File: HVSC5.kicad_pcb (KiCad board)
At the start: 2 copper layers, 220 x 152 mm, 336 parts, among them J1 test, J10 CONN_01X03, J11 test, J12 test, J13 test, J14 test, J15 test, J16 test, J17 CONN_COAXIAL, J18 CONN_01X03, J19 CONN_01X03, J2 test, J20 CONN_01X08, J21 test, J22 test, J23 test, J24 test, J25 CONN_01X05, J26 test, J27 test, J3 test, J4 test, J5 CONN_01X05, J6 test, J7 CONN_01X05, J8 CONN_COAXIAL, J9 DB9_Female_MountingHoles, SW1 SW_Push, U1 AD7175-8, U10 LT1118-5V, U11 FOD0721, U12 DPBW06, U13 LTC2644, U14 uA7805, U15 INA128, U16 XR2206, U17 TLP176A, U18 ANA4522, U19 ACPL-W343, U2 ADR4520, U20 ACPL-W343, U21 ANA4522, U3 ADR445, U4 74LS04, U5 dsPIC33EV256GM002, U6 SN75451, U7 MAX232, U8 HFBR-2412, U9 HFBR-1414, X1 P7002SCLRP, X2 P7002SCLRP, X3 P7002SCLRP, X4 P7002SCLRP, X5 P7002SCLRP, X6 P7002SCLRP, Y1 16M, Y2 8M

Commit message: Small_Change
시험삼아서 수정하였음
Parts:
- U2, U3: footprint Housings_SOIC:SOIC-8_3.9x4.9mm_Pitch1.27mm -> USER:SOIC-8_3.9x4.9mm_Pitch1.27mm
- moved J2 0.51 mm to (131.1, 79.5)
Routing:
- net /Monitor/Sine_output: track 59.2 -> 61.4 mm
- net Net-(R136-Pad1): track 15.2 -> 13.6 mm
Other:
- board text added: "+10V"
- board text added: "+1V"
- board text added: "+30V"
- board text added: "+600V"
- board text added: "-10V"
- board text added: "-1V"
- board text added: "-30V"
- board text added: "-600V"
- board text added: "Input+"
- board text added: "Input-"
- board text added: "Monitor"

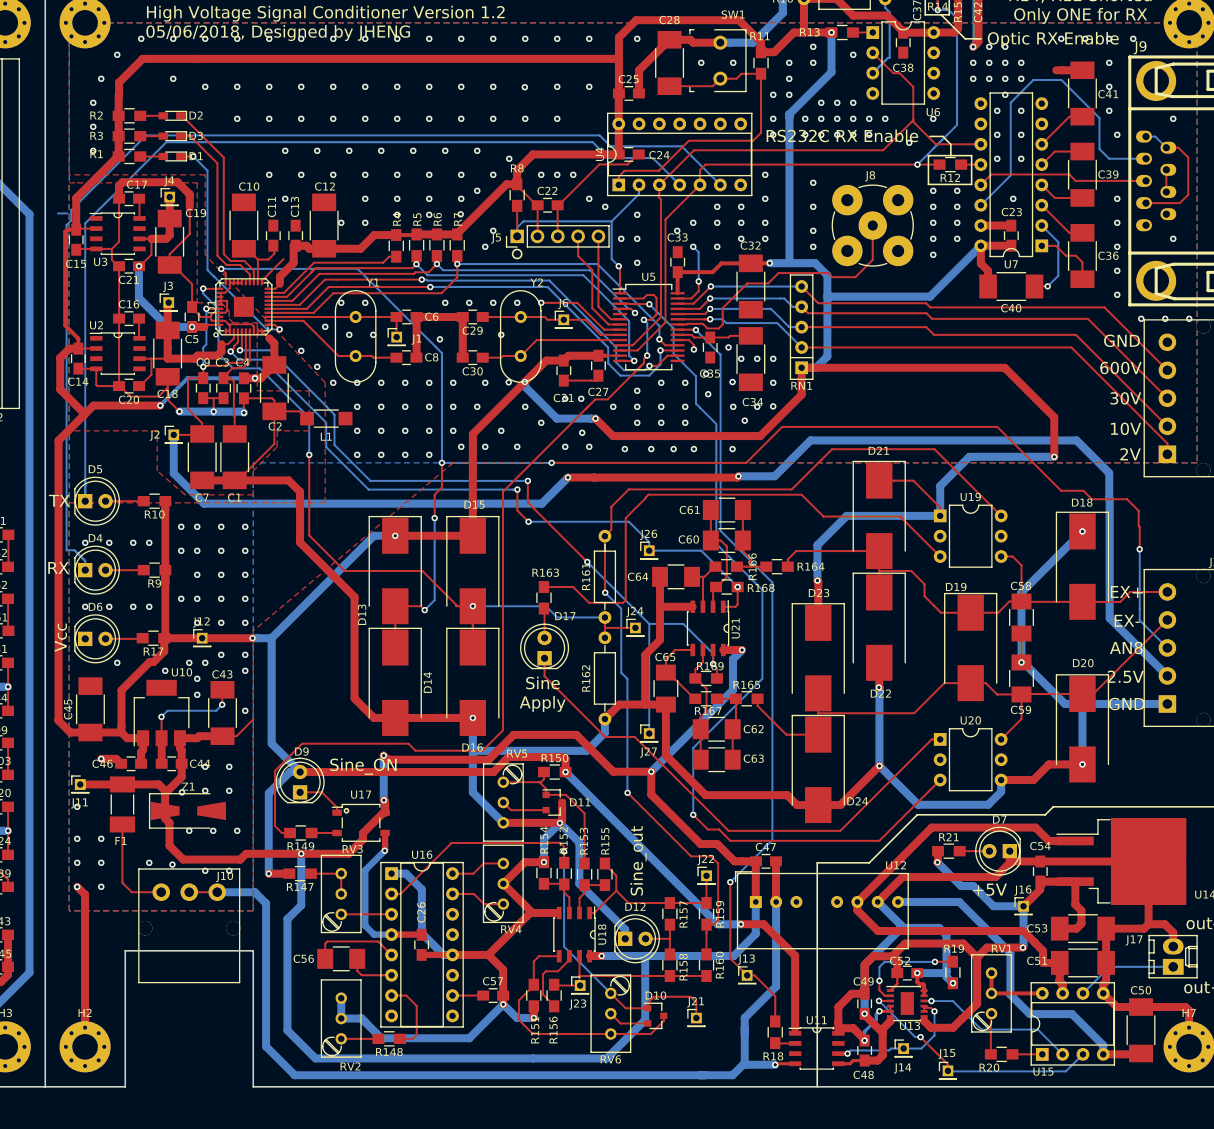
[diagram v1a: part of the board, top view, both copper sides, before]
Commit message: 전해콘덴서 foot print 변경
전해 콘덴서 변경
Bypass 콘데서 OPAMP에 추가 하여야 함
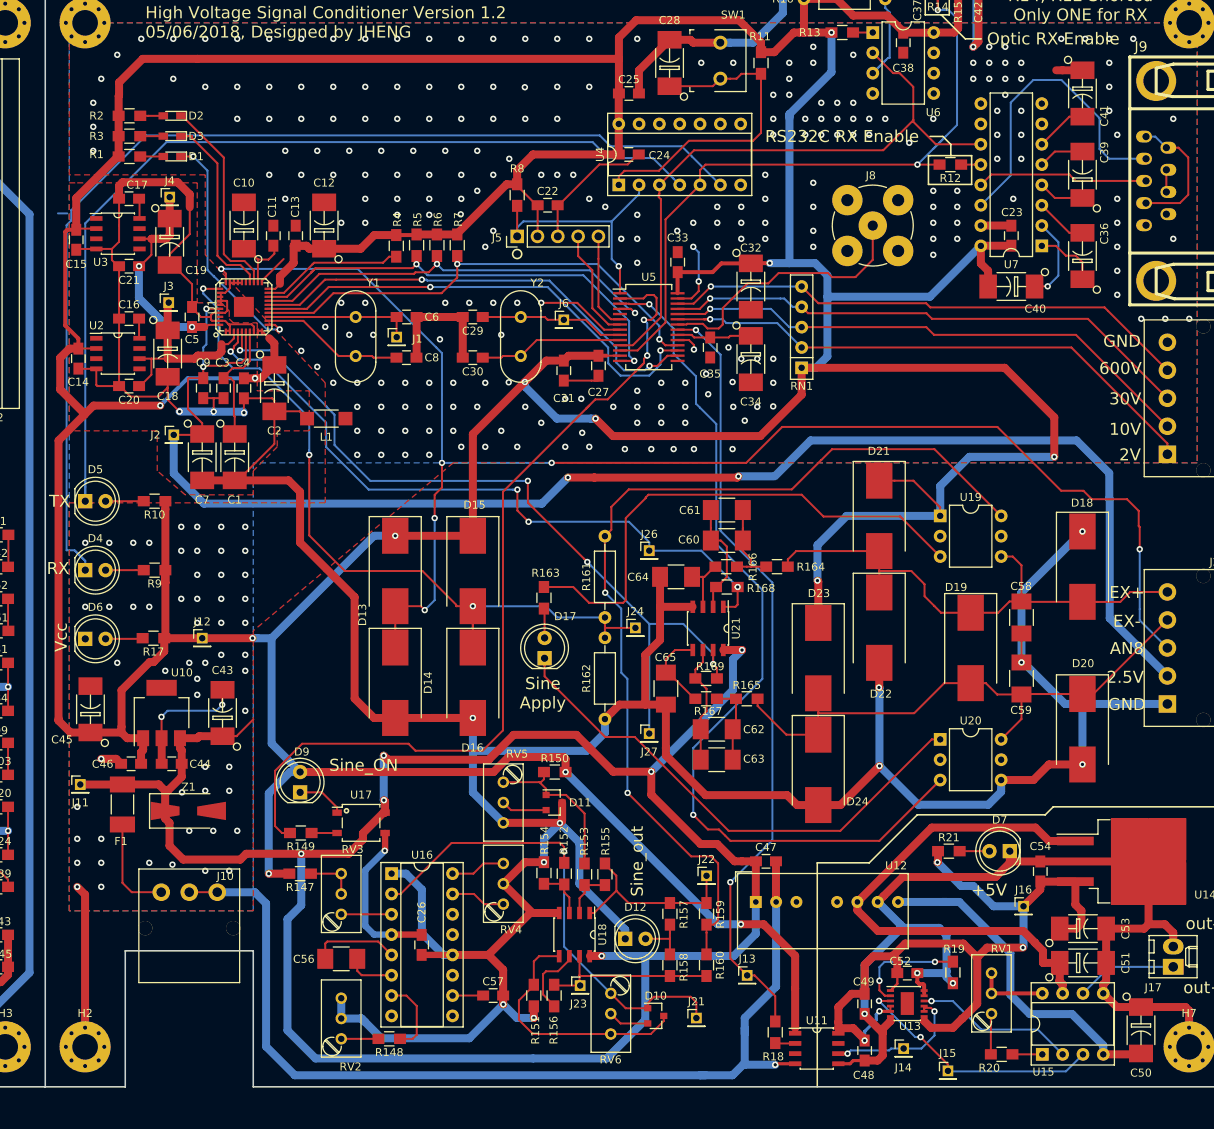
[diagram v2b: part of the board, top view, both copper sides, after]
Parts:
- C1, C10, C12, C18, C19, C2, C28, C32, C34, C36, C39, C40, C41, C43, C45, C50, C51, C53, C7: footprint Capacitors_SMD:C_1812_HandSoldering -> USER:C_1812_HandSoldering_Polar
- C55: value 0.1uF -> 10uF
- R159, R160: value 10k -> 1k

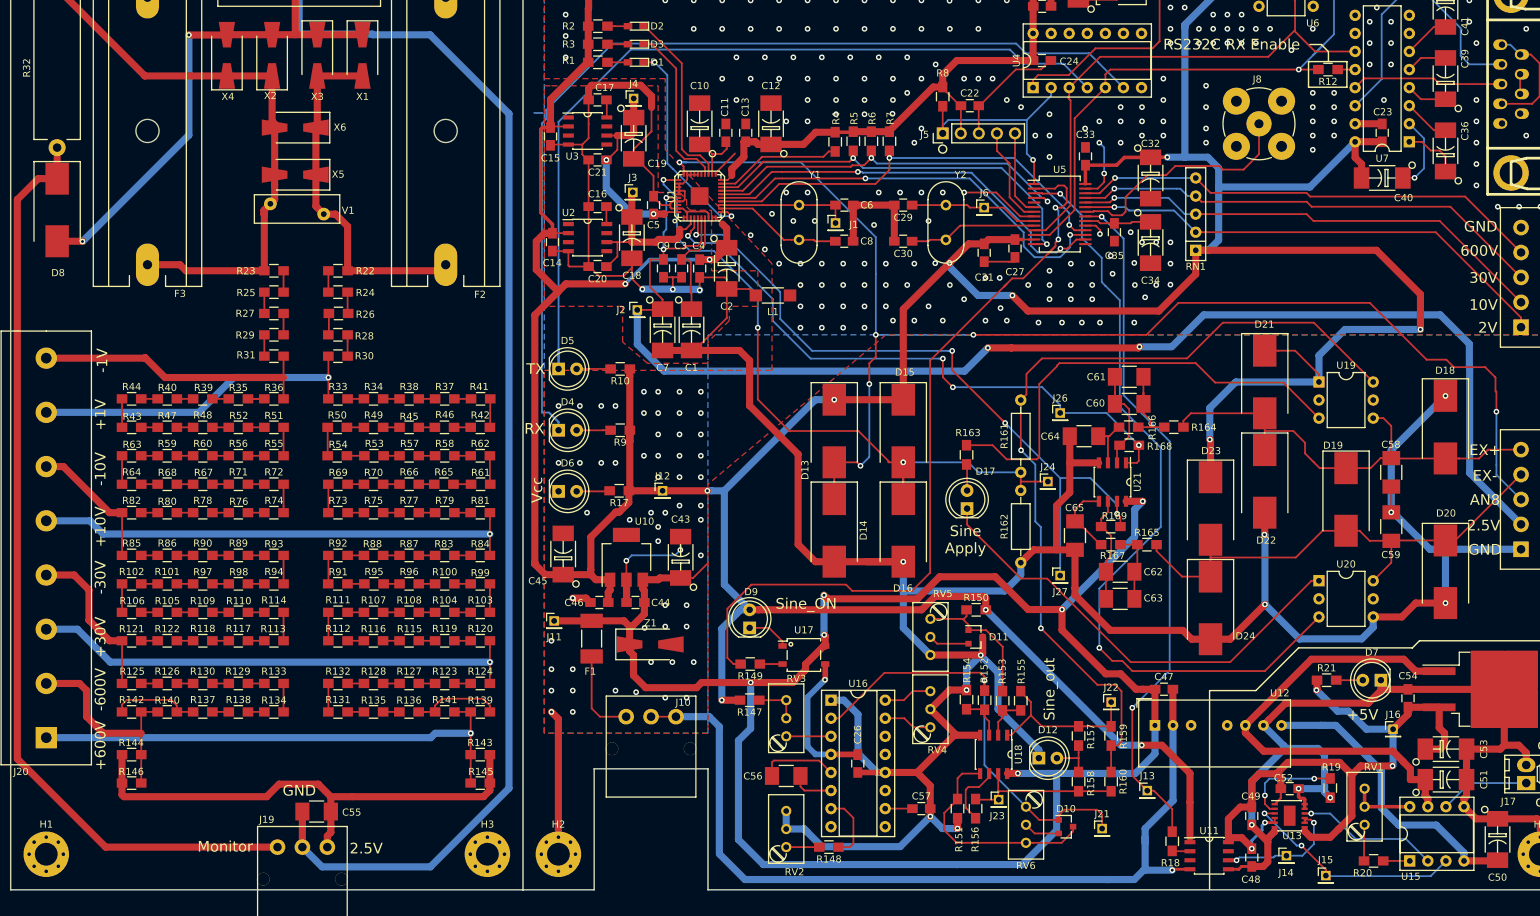
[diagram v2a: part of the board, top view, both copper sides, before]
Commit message: 2차 PCB 1차 수정
1. ADR455 Vcc V12 수정
2. DCDC 입력전압 변경
3. Bypass 콘덴서 C66, C67 추가
4. SOIC 방향 표시
5. TLV431 PADS 변경
6. AQV258 Pin3 --> Pin2
7. 전해콘덴서 방향추가
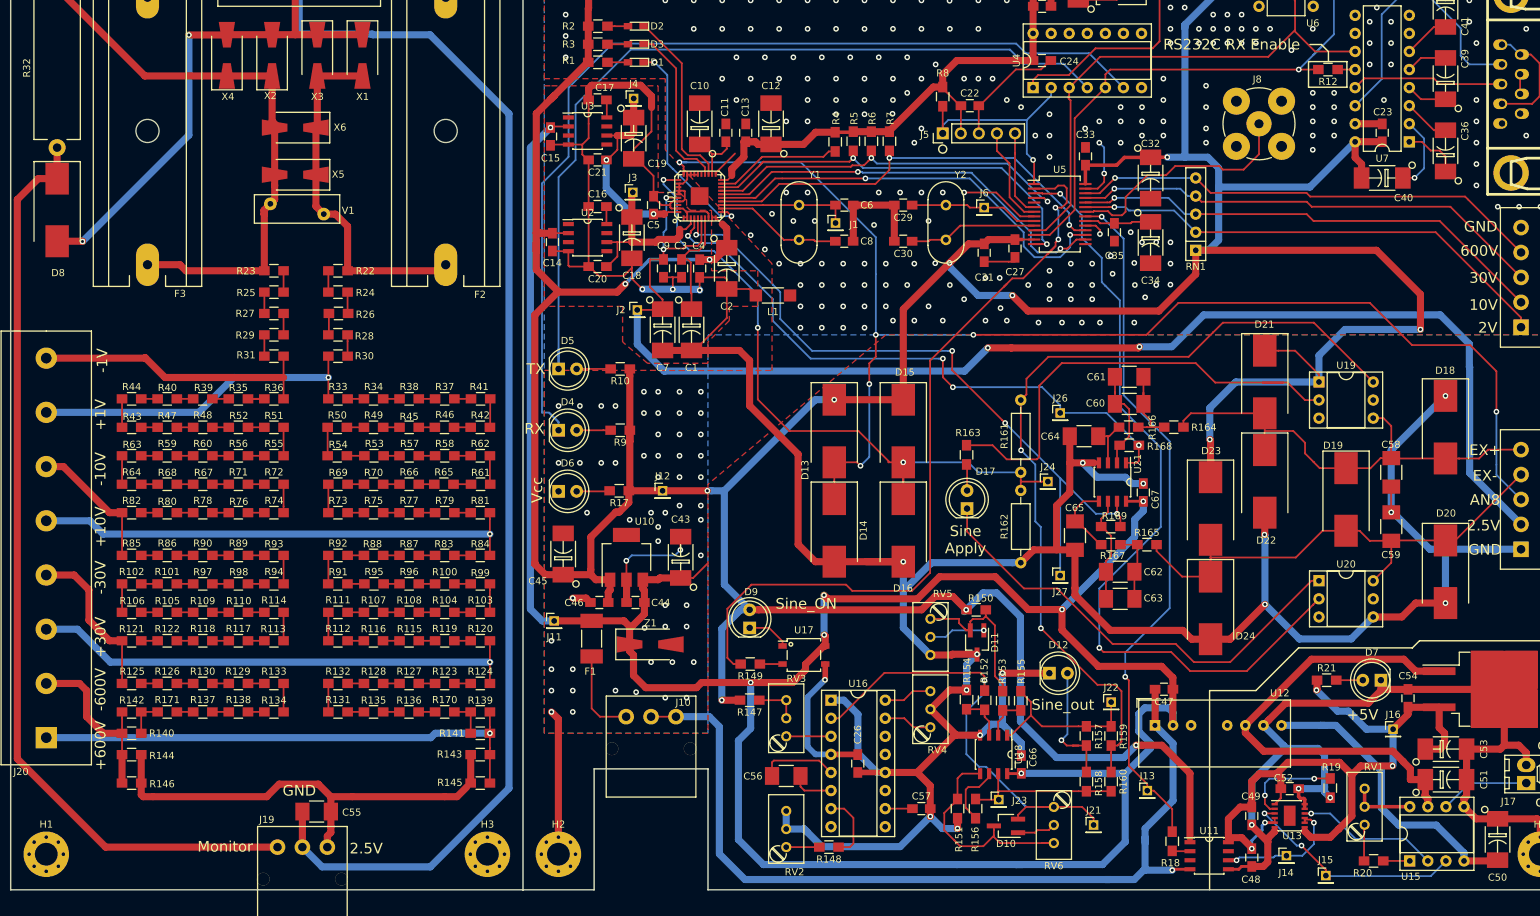
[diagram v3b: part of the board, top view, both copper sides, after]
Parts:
- added C66: 0.1uF, Capacitors_SMD:C_0805_HandSoldering, F.Cu at (185.0, 143.4)
- added C67: 0.1uF, Capacitors_SMD:C_0805_HandSoldering, F.Cu at (202.2, 105.2)
- added R170: 10k, Resistors_SMD:R_0805_HandSoldering, F.Cu at (104.0, 136.0)
- added R171: 10k, Resistors_SMD:R_0805_HandSoldering, F.Cu at (65.0, 136.0)
- D10, D11: footprint TO_SOT_Packages_SMD:SOT-23 -> USER:SOT-23W_Handsoldering(LM431)
- R163: value 220 -> 100
- U19, U20: value ACPL-W343 -> AQV258; footprint Housings_DIP:DIP-6_W7.62mm -> Housings_DIP:DIP-6_W7.62mm_Socket
- moved D12 12.0 mm to (189.0, 130.6)
- moved D10 8.43 mm to (182.9, 152.0), turned to 180 degrees
- moved R140 5.83 mm to (60.0, 139.0)
- moved R141 5.83 mm to (109.0, 139.0)
- moved RV6 3.92 mm to (189.6, 149.4)
- moved J21 1.29 mm to (195.2, 151.9)
- moved R157 1.10 mm to (194.2, 139.4)
- moved R158 1.10 mm to (194.2, 145.8)
- moved D11 0.80 mm to (178.8, 126.2), turned to 270 degrees
- turned C47 to 180 degrees
- turned R139 to 0 degrees
- turned R142 to 180 degrees
- turned R143 to 0 degrees
- turned R144 to 180 degrees
- turned R145 to 0 degrees
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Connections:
- C15 pad 1: VCC -> +12V
- R139 pad 1: Net-(R136-Pad1) -> Net-(R139-Pad1)
- R140 pad 1: Net-(R137-Pad1) -> Net-(R140-Pad1)
- R141 pad 1: Net-(R136-Pad1) -> Net-(R139-Pad1)
- R142 pad 1: Net-(R137-Pad1) -> Net-(R140-Pad1)
- U12 pad 1: +12V -> GND
- U12 pad 2: GND -> +12V
- U19 pad 2: Net-(U19-Pad2) -> Net-(R163-Pad2)
- U19 pad 3: Net-(R163-Pad2) -> Net-(U19-Pad3)
- U20 pad 2: Net-(U20-Pad2) -> /Voltage_Divider/Wire_Break
- U20 pad 3: /Voltage_Divider/Wire_Break -> Net-(U20-Pad3)
- U3 pad 2: VCC -> +12V
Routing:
- net +12V: track 264.5 -> 363.5 mm, vias 6 -> 7
- net Net-(D12-Pad2): track 6.76 -> 18.1 mm, vias 0 -> 1
- net Net-(R136-Pad1): track 13.6 -> 2.32 mm
- net VCC: track 886.2 -> 896.8 mm
- net Net-(R137-Pad1): track 12.5 -> 2.30 mm
- net +2V5: track 260.8 -> 254.0 mm
- net /Monitor/Sine_output: track 61.4 -> 68.0 mm
- net Net-(R139-Pad1): track 0.00 -> 5.05 mm
- net Net-(R140-Pad1): track 0.00 -> 5.05 mm
- net /Passive_Network/N600V: track 30.7 -> 25.7 mm
- net Net-(D11-Pad1): track 20.1 -> 22.8 mm
- net GNDREF: track 827.6 -> 825.2 mm, vias 15 -> 20
- net Net-(D11-Pad2): track 5.74 -> 7.89 mm, vias 0 -> 1
- net Net-(R163-Pad2): track 65.2 -> 66.9 mm
- net (no net): track 1.16 -> 0.00 mm
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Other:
- net class Power: clearance 0.15 -> 0.2

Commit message: switch 수정
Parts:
- removed R12, R14: 0, Resistors_SMD:R_0805_HandSoldering
- added SW3: SW_DPDT_x2, USER:SW_E-Switch_EG2219_DPDT, F.Cu at (222.5, 49.0)
- U21: footprint USER:SOIC-8_3.9x4.9mm_Pitch1.27mm -> Housings_SOIC:SOIC-8-1EP_3.9x4.9mm_Pitch1.27mm
- moved J8 20.2 mm to (223.0, 73.0)
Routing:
- net /dSPIC33EV/RXD: track 88.3 -> 56.8 mm, vias 2 -> 0
- net Net-(C37-Pad1): track 12.0 -> 43.4 mm, vias 0 -> 1
- net Net-(SW3-Pad3): track 2.46 -> 13.9 mm
- net VCC: track 896.8 -> 886.5 mm, vias 13 -> 14
- net GND: track 328.4 -> 325.2 mm, vias 310 -> 306
- net Net-(J8-Pad1): track 34.1 -> 32.0 mm, vias 0 -> 1
- net /dSPIC33EV/TXD: track 79.2 -> 80.9 mm
- net Net-(J7-Pad1): track 69.3 -> 70.3 mm
- net Net-(J7-Pad2): track 67.6 -> 68.2 mm
- net (no net): vias 0 -> 1
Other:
- board text added: "RS232C Optic Selection"
- board text removed: "Optic RX Enable"
- board text removed: "R14, R12 Shorted Only ONE for RX"
- board text removed: "RS232C RX Enable"
